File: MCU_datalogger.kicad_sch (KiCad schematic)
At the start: 25 parts, among them U1 24LC1025, U2 DS1337S_, U3 24LC1025, U4 ATMEGA328P-AU, Y1 32.768 KHz, Y2 16 MHz

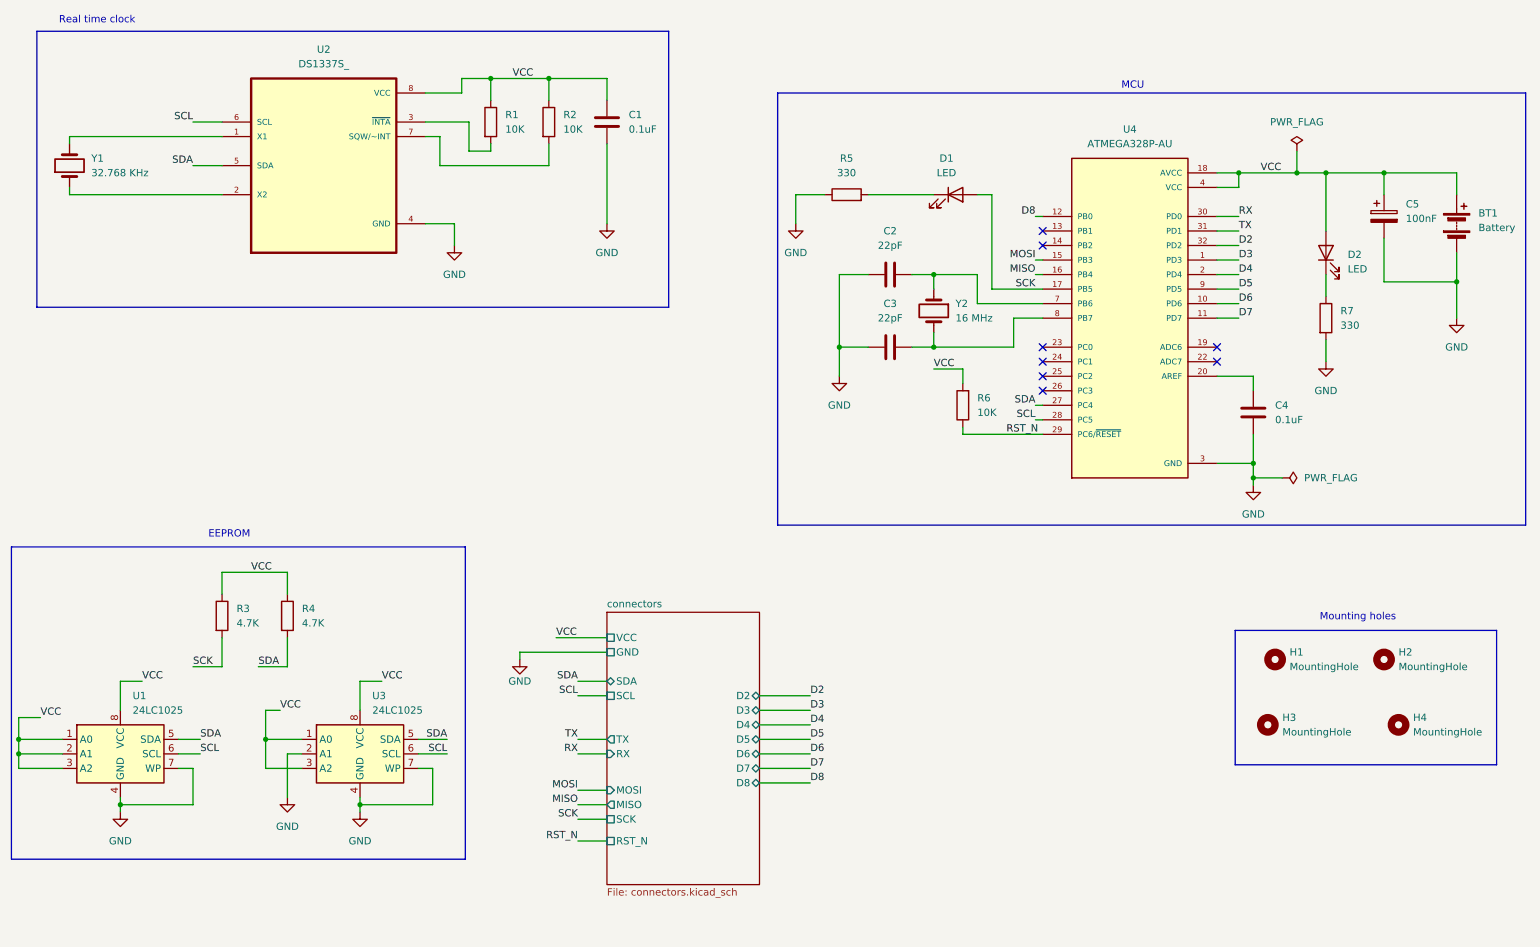
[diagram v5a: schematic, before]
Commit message: fixed scl/sck issue in layout
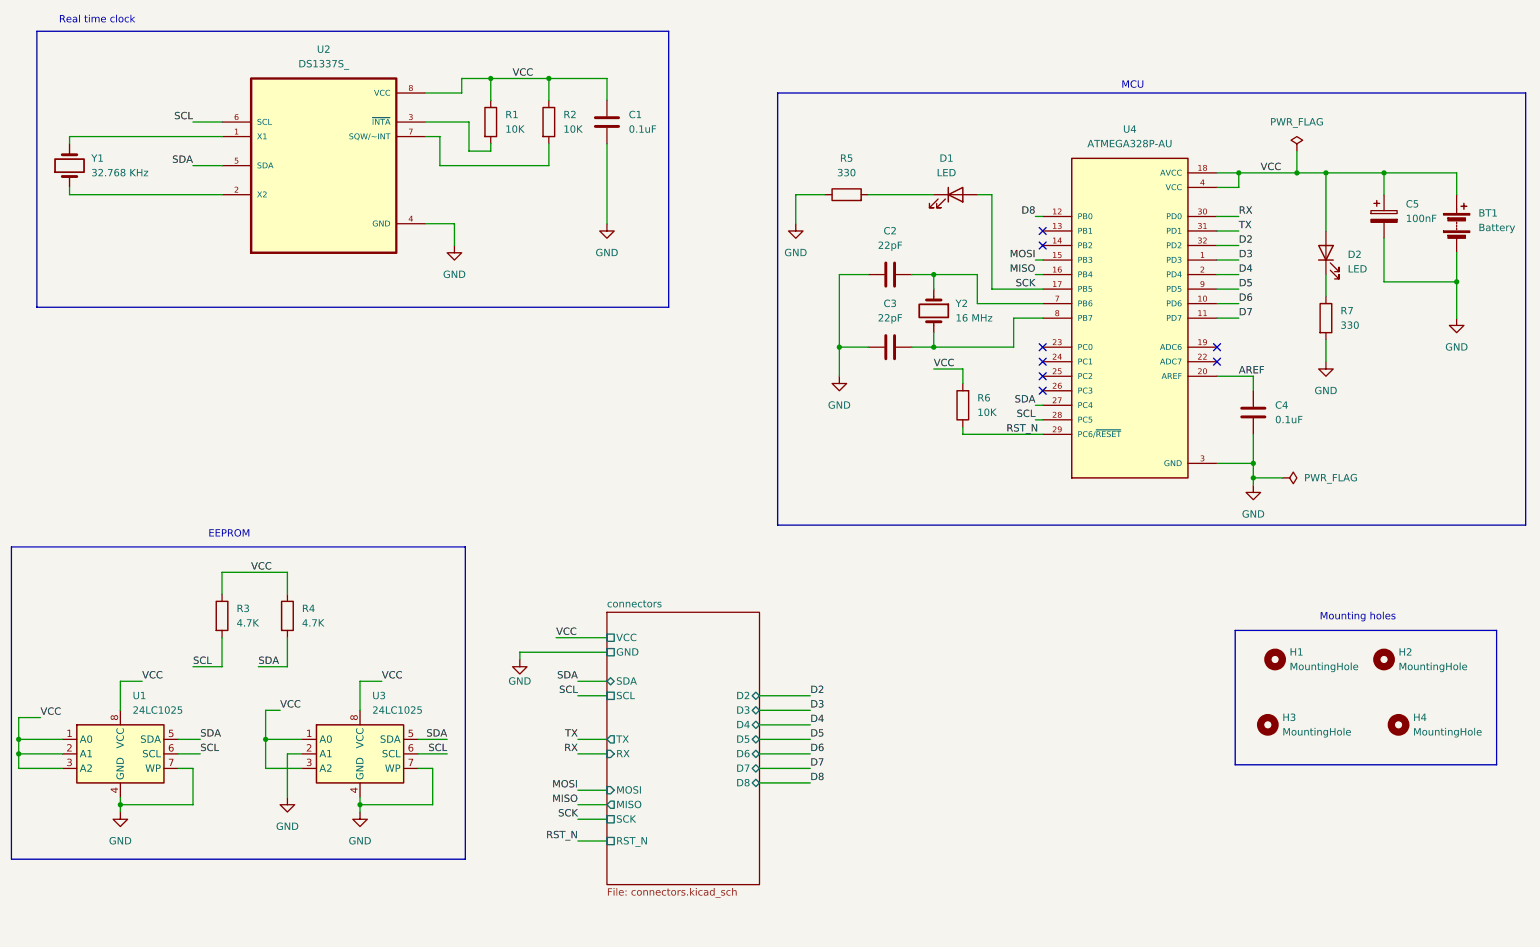
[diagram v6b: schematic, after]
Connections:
- net SCK: no longer R3.2
- net SCL: now also R3.2
- net AREF: now reaches C4.2, U4.20 (AREF)
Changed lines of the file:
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@@
 		)
 	)
-	(label "SCK"
+	(label "SCL"
 		(at 46.99 140.97 0)
 		(effects
@@
 		)
 	)
+	(label "AREF"
+		(at 229.87 90.17 0)
+		(effects
+			(font
+				(size 1.27 1.27)
+			)
+			(justify left bottom)
+		)
+	)
